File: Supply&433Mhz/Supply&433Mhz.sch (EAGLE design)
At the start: 17 parts, among them K1 61004021821, P1 DF11-06-2DSA, Q1 BS170

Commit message: Remove AGND supply, since DC/DC converter use same GND signal.
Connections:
- removed net AGND: 24V.1, MP1584-1.IN-, MP1584-2.IN-
- net GND: now also 24V.1, MP1584-1.IN-, MP1584-2.IN-
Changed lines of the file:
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@@
 <part name="GND1" library="supply1" deviceset="GND" device=""/>
 <part name="P+1" library="supply1" deviceset="+24V" device=""/>
-<part name="AGND1" library="supply1" deviceset="AGND" device=""/>
 <part name="GND2" library="supply1" deviceset="GND" device=""/>
 <part name="Q1" library="transistor-small-signal" deviceset="BS170" device="">
@@
 <part name="K1" library="Board_to_Board_Connectors_rev15d" deviceset="61004021821" device="" value="61004021821"/>
 <part name="RXB6" library="diy-modules" deviceset="WIRELESS-RXB6-5V" device=""/>
+<part name="GND3" library="supply1" deviceset="GND" device=""/>
 </parts>
 <sheets>
@@
 <attribute name="VALUE" x="35.56" y="78.74" size="1.778" layer="96" align="center-left"/>
 </instance>
-<instance part="AGND1" gate="VR1" x="22.86" y="63.5"/>
 <instance part="GND2" gate="1" x="114.3" y="17.78"/>
 <instance part="Q1" gate="1" x="129.54" y="66.04" smashed="yes" rot="R180">
@@
 <instance part="K1" gate="G$1" x="182.88" y="63.5" rot="MR0"/>
 <instance part="RXB6" gate="G$1" x="152.4" y="40.64" rot="MR0"/>
+<instance part="GND3" gate="1" x="22.86" y="63.5"/>
 </instances>
 <busses>
@@
 <wire x1="27.94" y1="78.74" x2="27.94" y2="58.42" width="0.1524" layer="91"/>
 <wire x1="20.32" y1="78.74" x2="27.94" y2="78.74" width="0.1524" layer="91"/>
-</segment>
-</net>
-<net name="AGND" class="0">
-<segment>
-<wire x1="22.86" y1="76.2" x2="22.86" y2="81.28" width="0.1524" layer="91"/>
-<wire x1="22.86" y1="81.28" x2="22.86" y2="88.9" width="0.1524" layer="91"/>
-<wire x1="22.86" y1="76.2" x2="22.86" y2="68.58" width="0.1524" layer="91"/>
-<pinref part="AGND1" gate="VR1" pin="AGND"/>
-<wire x1="22.86" y1="68.58" x2="22.86" y2="66.04" width="0.1524" layer="91"/>
-<pinref part="MP1584-2" gate="G$1" pin="IN-"/>
-<wire x1="22.86" y1="88.9" x2="35.56" y2="88.9" width="0.1524" layer="91"/>
-<pinref part="MP1584-1" gate="G$1" pin="IN-"/>
-<wire x1="22.86" y1="68.58" x2="35.56" y2="68.58" width="0.1524" layer="91"/>
-<junction x="22.86" y="68.58"/>
-<pinref part="24V" gate="G$1" pin="1"/>
-<wire x1="20.32" y1="81.28" x2="22.86" y2="81.28" width="0.1524" layer="91"/>
-<junction x="22.86" y="81.28"/>
 </segment>
 </net>
@@
 <junction x="119.38" y="38.1"/>
 </segment>
+<segment>
+<wire x1="22.86" y1="76.2" x2="22.86" y2="81.28" width="0.1524" layer="91"/>
+<wire x1="22.86" y1="81.28" x2="22.86" y2="88.9" width="0.1524" layer="91"/>
+<wire x1="22.86" y1="76.2" x2="22.86" y2="68.58" width="0.1524" layer="91"/>
+<wire x1="22.86" y1="68.58" x2="22.86" y2="66.04" width="0.1524" layer="91"/>
+<pinref part="MP1584-2" gate="G$1" pin="IN-"/>
+<wire x1="22.86" y1="88.9" x2="35.56" y2="88.9" width="0.1524" layer="91"/>
+<pinref part="MP1584-1" gate="G$1" pin="IN-"/>
+<wire x1="22.86" y1="68.58" x2="35.56" y2="68.58" width="0.1524" layer="91"/>
+<junction x="22.86" y="68.58"/>
+<pinref part="24V" gate="G$1" pin="1"/>
+<wire x1="20.32" y1="81.28" x2="22.86" y2="81.28" width="0.1524" layer="91"/>
+<junction x="22.86" y="81.28"/>
+<pinref part="GND3" gate="1" pin="GND"/>
+</segment>
 </net>

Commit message: Change protection diode from 1N4148 to BS160.
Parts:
- D3, D4: value 1N4148DO35-7 -> SB160; device diode:1N4148DO35-7 -> diode:DIODE-DO41-7.6
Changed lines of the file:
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@@
 <part name="MP1584-2" library="diy-modules" deviceset="DC-DC-STEP-DOWN-MP1584" device=""/>
 <part name="MP1584-1" library="diy-modules" deviceset="DC-DC-STEP-DOWN-MP1584" device=""/>
-<part name="D3" library="diode" deviceset="1N4148" device="DO35-7"/>
-<part name="D4" library="diode" deviceset="1N4148" device="DO35-7"/>
+<part name="D3" library="diode" deviceset="DIODE-" device="DO41-7.6" value="SB160"/>
+<part name="D4" library="diode" deviceset="DIODE-" device="DO41-7.6" value="SB160"/>
 <part name="C1" library="capacitor-wima" deviceset="C" device="2,5-3" value="100nF"/>
 <part name="K1" library="Board_to_Board_Connectors_rev15d" deviceset="61004021821" device="" value="61004021821"/>

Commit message: Use SB1H100 as protection diode instead of SB160.
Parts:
- D3, D4: value SB160 -> SB1H100
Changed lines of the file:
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@@
 <part name="MP1584-2" library="diy-modules" deviceset="DC-DC-STEP-DOWN-MP1584" device=""/>
 <part name="MP1584-1" library="diy-modules" deviceset="DC-DC-STEP-DOWN-MP1584" device=""/>
-<part name="D3" library="diode" deviceset="DIODE-" device="DO41-7.6" value="SB160"/>
-<part name="D4" library="diode" deviceset="DIODE-" device="DO41-7.6" value="SB160"/>
+<part name="D3" library="diode" deviceset="DIODE-" device="DO41-7.6" value="SB1H100"/>
+<part name="D4" library="diode" deviceset="DIODE-" device="DO41-7.6" value="SB1H100"/>
 <part name="C1" library="capacitor-wima" deviceset="C" device="2,5-3" value="100nF"/>
 <part name="K1" library="Board_to_Board_Connectors_rev15d" deviceset="61004021821" device="" value="61004021821"/>

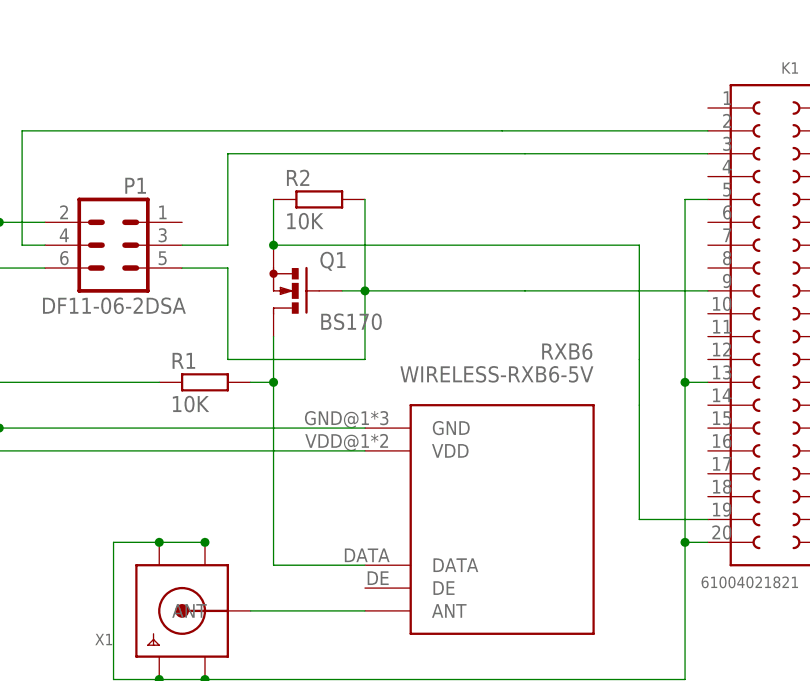
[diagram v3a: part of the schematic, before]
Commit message: Use 1K as pull-up instead of 10K.
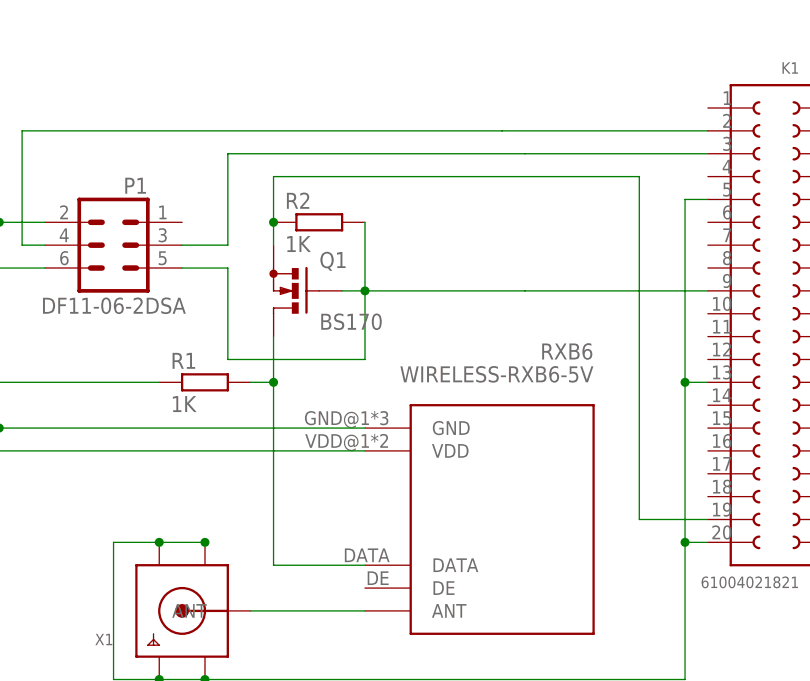
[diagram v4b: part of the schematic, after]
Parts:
- R1, R2: value 10K -> 1K
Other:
- moved on the sheet: R2
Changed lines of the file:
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@@
 <attribute name="OC_FARNELL" value="9556192"/>
 </part>
-<part name="R2" library="rcl" deviceset="R-EU_" device="0204/2V" value="10K">
+<part name="R2" library="rcl" deviceset="R-EU_" device="0204/2V" value="1K">
 <attribute name="MF" value=""/>
 <attribute name="MPN" value=""/>
 <attribute name="OC_FARNELL" value="unknown"/>
 </part>
-<part name="R1" library="rcl" deviceset="R-EU_" device="0204/2V" value="10K">
+<part name="R1" library="rcl" deviceset="R-EU_" device="0204/2V" value="1K">
 <attribute name="MF" value=""/>
 <attribute name="MPN" value=""/>
@@
 <attribute name="VALUE" x="132.08" y="63.5" size="1.778" layer="96" rot="R180" align="bottom-right"/>
 </instance>
-<instance part="R2" gate="G$1" x="132.08" y="76.2">
-<attribute name="OC_FARNELL" x="132.08" y="76.2" size="1.778" layer="96" rot="R270" display="off"/>
-<attribute name="MF" x="132.08" y="76.2" size="1.778" layer="96" rot="R270" display="off"/>
-<attribute name="MPN" x="132.08" y="76.2" size="1.778" layer="96" rot="R270" display="off"/>
+<instance part="R2" gate="G$1" x="132.08" y="73.66">
+<attribute name="OC_FARNELL" x="132.08" y="73.66" size="1.778" layer="96" rot="R270" display="off"/>
+<attribute name="MF" x="132.08" y="73.66" size="1.778" layer="96" rot="R270" display="off"/>
+<attribute name="MPN" x="132.08" y="73.66" size="1.778" layer="96" rot="R270" display="off"/>
 </instance>
 <instance part="R1" gate="G$1" x="119.38" y="55.88">
@@
 <segment>
 <pinref part="Q1" gate="1" pin="S"/>
-<wire x1="127" y1="71.12" x2="167.64" y2="71.12" width="0.1524" layer="91"/>
-<wire x1="167.64" y1="71.12" x2="167.64" y2="58.42" width="0.1524" layer="91"/>
-<wire x1="127" y1="76.2" x2="127" y2="71.12" width="0.1524" layer="91"/>
-<junction x="127" y="71.12"/>
+<wire x1="127" y1="71.12" x2="127" y2="73.66" width="0.1524" layer="91"/>
+<wire x1="127" y1="73.66" x2="127" y2="78.74" width="0.1524" layer="91"/>
+<wire x1="127" y1="78.74" x2="167.64" y2="78.74" width="0.1524" layer="91"/>
+<wire x1="167.64" y1="78.74" x2="167.64" y2="40.64" width="0.1524" layer="91"/>
 <pinref part="R2" gate="G$1" pin="1"/>
-<wire x1="167.64" y1="58.42" x2="167.64" y2="53.34" width="0.1524" layer="91"/>
-<wire x1="167.64" y1="53.34" x2="167.64" y2="40.64" width="0.1524" layer="91"/>
 <pinref part="K1" gate="G$1" pin="19"/>
 <wire x1="167.64" y1="40.64" x2="175.26" y2="40.64" width="0.1524" layer="91"/>
+<junction x="127" y="73.66"/>
 </segment>
 </net>
@@
 <pinref part="Q1" gate="1" pin="G"/>
 <wire x1="134.62" y1="66.04" x2="137.16" y2="66.04" width="0.1524" layer="91"/>
-<wire x1="137.16" y1="66.04" x2="137.16" y2="76.2" width="0.1524" layer="91"/>
+<wire x1="137.16" y1="66.04" x2="137.16" y2="73.66" width="0.1524" layer="91"/>
 <pinref part="P1" gate="G$1" pin="5"/>
 <wire x1="116.84" y1="68.58" x2="121.92" y2="68.58" width="0.1524" layer="91"/>

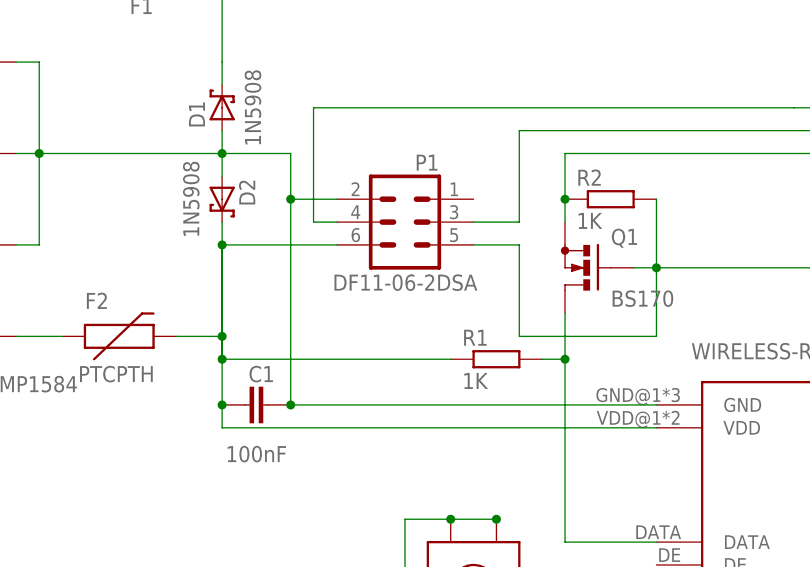
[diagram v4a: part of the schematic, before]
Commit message: Replace package for DF11 connector.
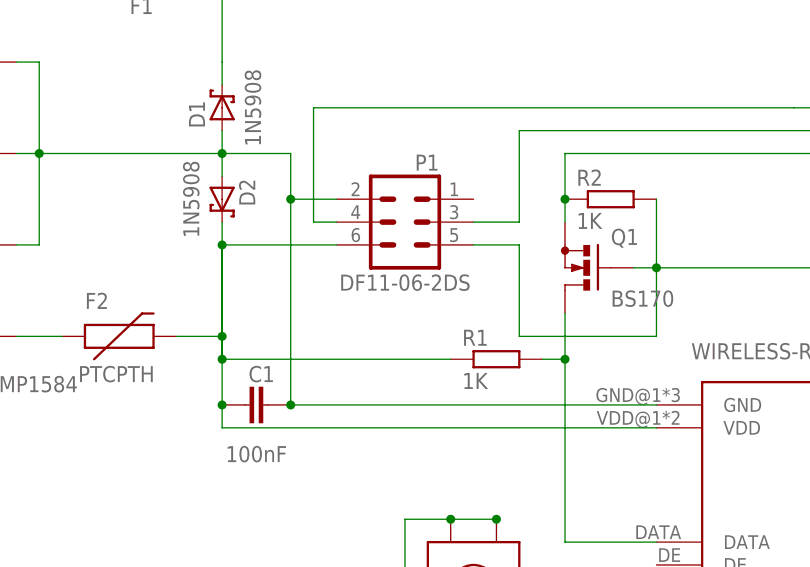
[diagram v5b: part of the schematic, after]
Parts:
- P1: value DF11-06-2DSA -> DF11-06-2DS; device con-hirose-df11:DF11-06-2DSA -> con-hirose-df11:DF11-06-2DS
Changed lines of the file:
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@@
 <parts>
 <part name="X1" library="adafruit" deviceset="SMACONNECTOR" device=""/>
-<part name="P1" library="con-hirose-df11" deviceset="DF11-06-2DSA" device=""/>
+<part name="P1" library="con-hirose-df11" deviceset="DF11-06-2" device="DS" value="DF11-06-2DS"/>
 <part name="24V" library="con-wuerth" deviceset="691131710002" device=""/>
 <part name="D1" library="diode" deviceset="1N5908" device=""/>
